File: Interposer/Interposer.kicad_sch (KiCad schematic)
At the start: 11 parts, among them J1 Cis_Electrode_In, J10 Trans_Electrode_Out, J11 Trans_Electrode_In, J2 Cis_Electrode_Out, P1 Port_Cis_In_30deg, P2 Port_Cis_Out_330deg, P3 Port_Trans_In_210deg, P4 Port_Trans_Out_150deg

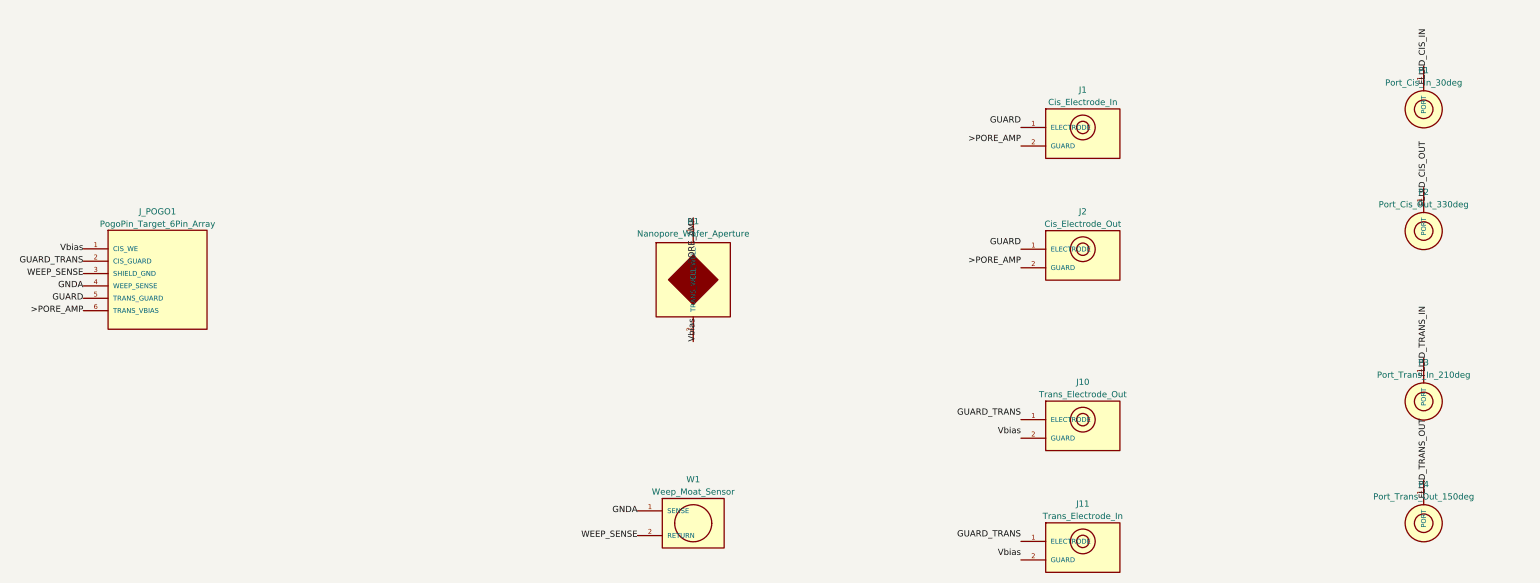
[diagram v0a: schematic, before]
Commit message: feat(interposer): implement 4-electrode concentric cell with Gamry terminology, EIS simulation, and KiCad models
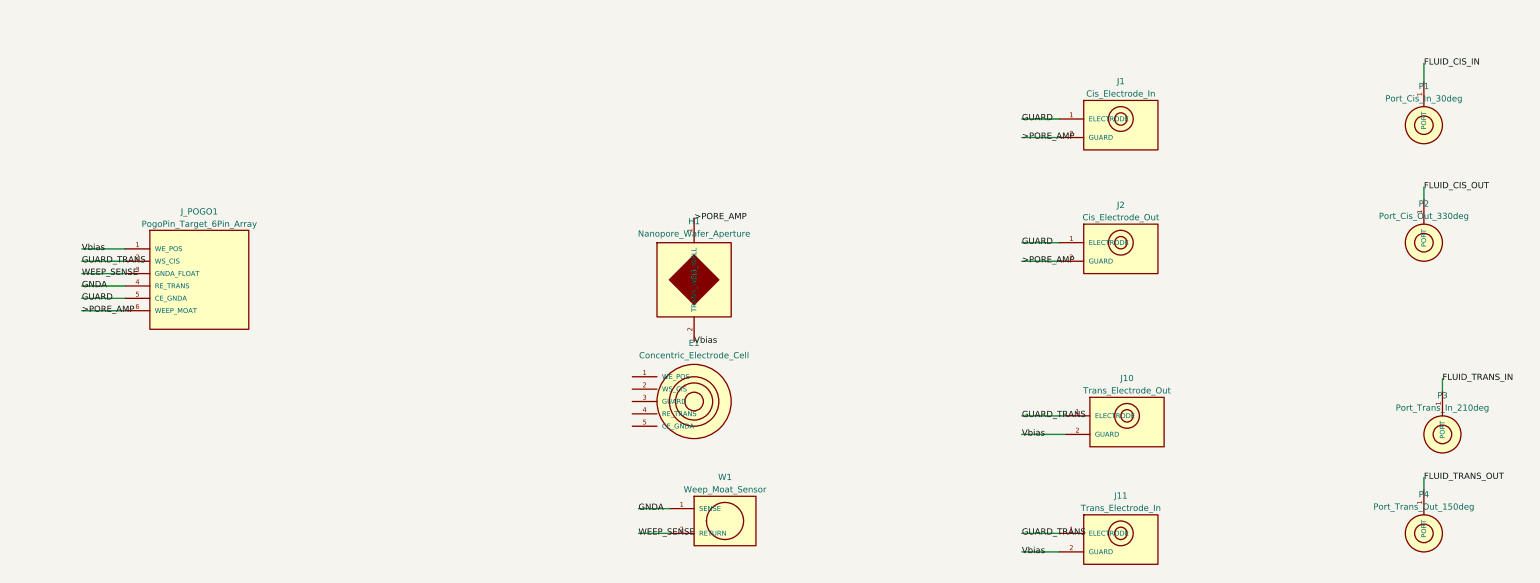
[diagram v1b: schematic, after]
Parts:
- added E1: Concentric_Electrode_Cell, footprints:Nanopore holder_recessed, symbol Interposer:Concentric_Electrode_Cell
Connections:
- net >PORE_AMP: now also J1.2 (GUARD), J2.2 (GUARD)
- net FLUID_CIS_IN: now also P1.1 (PORT)
- net FLUID_CIS_OUT: now also P2.1 (PORT)
- net FLUID_TRANS_IN: now also P3.1 (PORT)
- net FLUID_TRANS_OUT: now also P4.1 (PORT)
- net GUARD: now also J1.1 (ELECTRODE), J2.1 (ELECTRODE)
- net GUARD_TRANS: now also J10.1 (ELECTRODE), J11.1 (ELECTRODE)
- net Vbias: now also J10.2 (GUARD), J11.2 (GUARD)
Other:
- moved on the sheet: J1, J10, J11, J2, J_POGO1, P1, P2, P3, P4, W1

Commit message: refactor(interposer): reconcile 4-electrode cell with channel-aligned Ag/AgCl ribbons and Gamry pinout
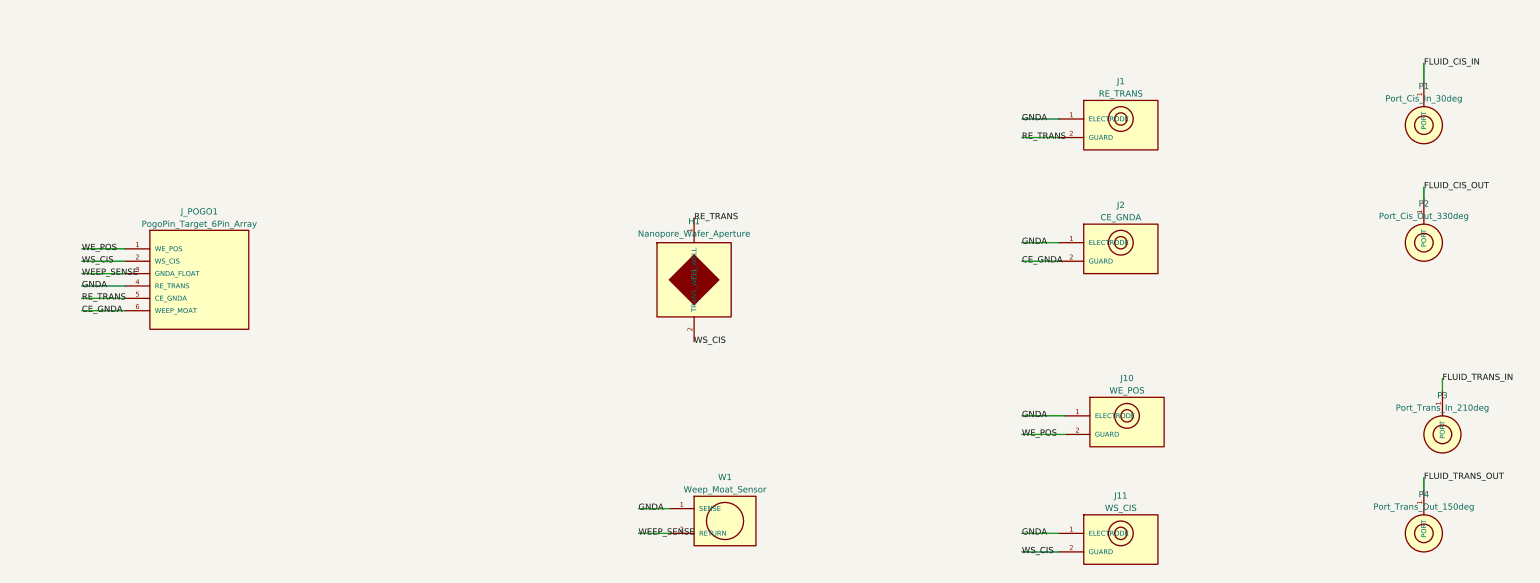
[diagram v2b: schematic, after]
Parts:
- removed E1: Concentric_Electrode_Cell, footprints:Nanopore holder_recessed, symbol Interposer:Concentric_Electrode_Cell
- J1: value Cis_Electrode_In -> RE_TRANS
- J10: value Trans_Electrode_Out -> WE_POS
- J11: value Trans_Electrode_In -> WS_CIS
- J2: value Cis_Electrode_Out -> CE_GNDA
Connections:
- net GNDA: now also J1.1 (ELECTRODE), J10.1 (ELECTRODE), J11.1 (ELECTRODE), J2.1 (ELECTRODE)
- net >PORE_AMP renamed CE_GNDA
- net CE_GNDA: no longer H1.1 (CIS_WELL), J1.2 (GUARD)
- removed net GUARD: J1.1 (ELECTRODE), J2.1 (ELECTRODE), J_POGO1.5 (CE_GNDA)
- removed net GUARD_TRANS: J10.1 (ELECTRODE), J11.1 (ELECTRODE), J_POGO1.2 (WS_CIS)
- net Vbias renamed WE_POS
- net WE_POS: no longer H1.2 (TRANS_WELL), J11.2 (GUARD)
- new net RE_TRANS: H1.1 (CIS_WELL), J1.2 (GUARD), J_POGO1.5 (CE_GNDA)
- new net WS_CIS: H1.2 (TRANS_WELL), J11.2 (GUARD), J_POGO1.2 (WS_CIS)
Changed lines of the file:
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@@
 		)
 	)
-	(label ">PORE_AMP"
+	(label "RE_TRANS"
 		(at 170.18 67.31 0)
 		(effects
@@
 		)
 	)
-	(label "GUARD_TRANS"
+	(label "GNDA"
 		(at 237.49 107.95 0)
 		(effects
@@
 		)
 	)
-	(label "Vbias"
+	(label "WS_CIS"
 		(at 237.49 135.89 0)
 		(effects
@@
 		)
 	)
-	(label ">PORE_AMP"
+	(label "CE_GNDA"
 		(at 237.49 76.2 0)
 		(effects
@@
 		)
 	)
-	(label "GUARD"
+	(label "RE_TRANS"
 		(at 44.45 83.82 0)
 		(effects
@@
 		)
 	)
-	(label "Vbias"
+	(label "WE_POS"
 		(at 44.45 73.66 0)
 		(effects
@@
 		)
 	)
-	(label "Vbias"
+	(label "WS_CIS"
 		(at 170.18 92.71 0)
 		(effects
@@
 		)
 	)
-	(label ">PORE_AMP"
+	(label "RE_TRANS"
 		(at 237.49 50.8 0)
 		(effects
@@
 		)
 	)
-	(label "GUARD"
+	(label "GNDA"
 		(at 237.49 46.99 0)
 		(effects
@@
 		)
 	)
-	(label "Vbias"
+	(label "WE_POS"
 		(at 237.49 111.76 0)
 		(effects
@@
 		)
 	)
-	(label "GUARD_TRANS"
+	(label "GNDA"
 		(at 237.49 132.08 0)
 		(effects
@@
 		)
 	)
-	(label ">PORE_AMP"
+	(label "CE_GNDA"
 		(at 44.45 86.36 0)
 		(effects
@@
 		)
 	)
-	(label "GUARD_TRANS"
+	(label "WS_CIS"
 		(at 44.45 76.2 0)
 		(effects
@@
 		)
 	)
-	(label "GUARD"
+	(label "GNDA"
 		(at 237.49 72.39 0)
 		(effects
@@
 			)
 		)
-		(property "Value" "Cis_Electrode_Out"
+		(property "Value" "CE_GNDA"
 			(at 257.81 67.2 0)
 			(show_name no)
@@
 			)
 		)
-		(property "Description" "Ag/AgCl Ribbon Electrode Pad (Cis Out, r=17mm) with Driven Guard Ring"
+		(property "Description" "Counter Electrode Pad (Ag/AgCl Ribbon, Trans Outer)"
 			(at 257.81 73.66 0)
 			(hide yes)
@@
 			)
 		)
-		(property "Value" "Cis_Electrode_In"
+		(property "Value" "RE_TRANS"
 			(at 257.81 41.8 0)
 			(show_name no)
@@
 			)
 		)
-		(property "Description" "Ag/AgCl Ribbon Electrode Pad (Cis In, r=12mm) with Driven Guard Ring"
+		(property "Description" "Reference Sense Electrode Pad (Ag/AgCl Ribbon, Trans Inner)"
 			(at 257.81 48.26 0)
 			(hide yes)
@@
 			)
 		)
-		(property "Value" "Trans_Electrode_In"
+		(property "Value" "WS_CIS"
 			(at 257.81 126.89 0)
 			(show_name no)
@@
 			)
 		)
-		(property "Description" "Ag/AgCl Ribbon Electrode Pad (Trans In, r=12mm) with Driven Guard Ring"
+		(property "Description" "Working Sense Electrode Pad (Ag/AgCl Ribbon, Cis Inner)"
 			(at 257.81 133.35 0)
 			(hide yes)
@@
 			)
 		)
-		(property "Value" "Trans_Electrode_Out"
+		(property "Value" "WE_POS"
 			(at 259.08 102.76 0)
 			(show_name no)
@@
 			)
 		)
-		(property "Description" "Ag/AgCl Ribbon Electrode Pad (Trans Out, r=17mm) with Driven Guard Ring"
+		(property "Description" "Working Electrode Pad (Ag/AgCl Ribbon, Cis Outer)"
 			(at 259.08 109.22 0)
 			(hide yes)
@@
 					(unit 1)
 				)
-			)
-		)
-	)
-	(symbol
-		(lib_id "Interposer:Concentric_Electrode_Cell")
-		(at 170.18 105.0 0)
-		(unit 1)
-		(body_style 1)
-		(exclude_from_sim no)
-		(in_bom yes)
-		(on_board yes)
-		(in_pos_files yes)
-		(dnp no)
-		(fields_autoplaced yes)
-		(property "Reference" "E1"
-			(at 170.18 93.0 0)
-			(show_name no)
-			(do_not_autoplace no)
-			(effects
-				(font
-					(size 1.27 1.27)
-				)
-			)
-		)
-		(property "Value" "Concentric_Electrode_Cell"
-			(at 170.18 95.54 0)
-			(show_name no)
-			(do_not_autoplace no)
-			(effects
-				(font
-					(size 1.27 1.27)
-				)
-			)
-		)
-		(property "Footprint" "footprints:Nanopore holder_recessed"
-			(at 170.18 105.0 0)
-			(hide yes)
-			(show_name no)
-			(do_not_autoplace no)
-			(effects
-				(font
-					(size 1.27 1.27)
-				)
-			)
-		)
-		(property "Datasheet" "https://pubs.acs.org/doi/10.1021/acs.jpcc.6b12543"
-			(at 170.18 105.0 0)
-			(hide yes)
-			(show_name no)
-			(do_not_autoplace no)
-			(effects
-				(font
-					(size 1.27 1.27)
-				)
-			)
-		)
-		(property "Description" "Four-Electrode Concentric Kelvin Electrochemical Cell (WE, WS, RE, CE, Guard)"
-			(at 170.18 105.0 0)
-			(hide yes)
-			(show_name no)
-			(do_not_autoplace no)
-			(effects
-				(font
-					(size 1.27 1.27)
-				)
-			)
-		)
-		(pin "1"
-		)
-		(pin "2"
-		)
-		(pin "3"
-		)
-		(pin "4"
-		)
-		(pin "5"
-		)
-		(instances
-			(project "Interposer"
-				(path "/0fac162c-ca5e-4358-934a-30718aa12176"
-					(reference "E1")
-					(unit 1)
-				)

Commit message: Update Interposer and Amplifier interfaces to 12-pin Guarded Pogo layout
Modifies `J_POGO1` (the mechanical interface bridging the active amplifier and
passive flowcell interposer) from a 6-pin linear array to a 12-pin layout.

This 12-pin architecture surrounds the ultra-high impedance signals (`WS_CIS`
and `RE_TRANS`) with explicitly driven `GUARD` pins. By flanking these sensitive
nodes with driven low-impedance guards across the mechanical pogo connection,
stray surface leakage across the FR4 and mating interfaces is intercepted and
bootstrapped.

Changes:
- Replaced 6-pin target array footprints with `PogoPin_Target_12Pin_Distributed`.
- Replaced 6-pin spring header footprints with `PogoPin_SpringHeader_12Pin_Distributed`.
- Updated KiCad footprint `.kicad_mod` files to feature 12 pads.
- Updated `scripts/build_interposer_kicad.py` to instantiate the new 12-pin generic connector symbols and bind to the correct footprints.
- Updated unit test assertions in `tests/test_interposer_kicad.py` to expect the new pin counts, names, and symbol mappings.

Co-authored-by: google-labs-jules[bot] <161369871+google-labs-jules[bot]@users.noreply.github.com>
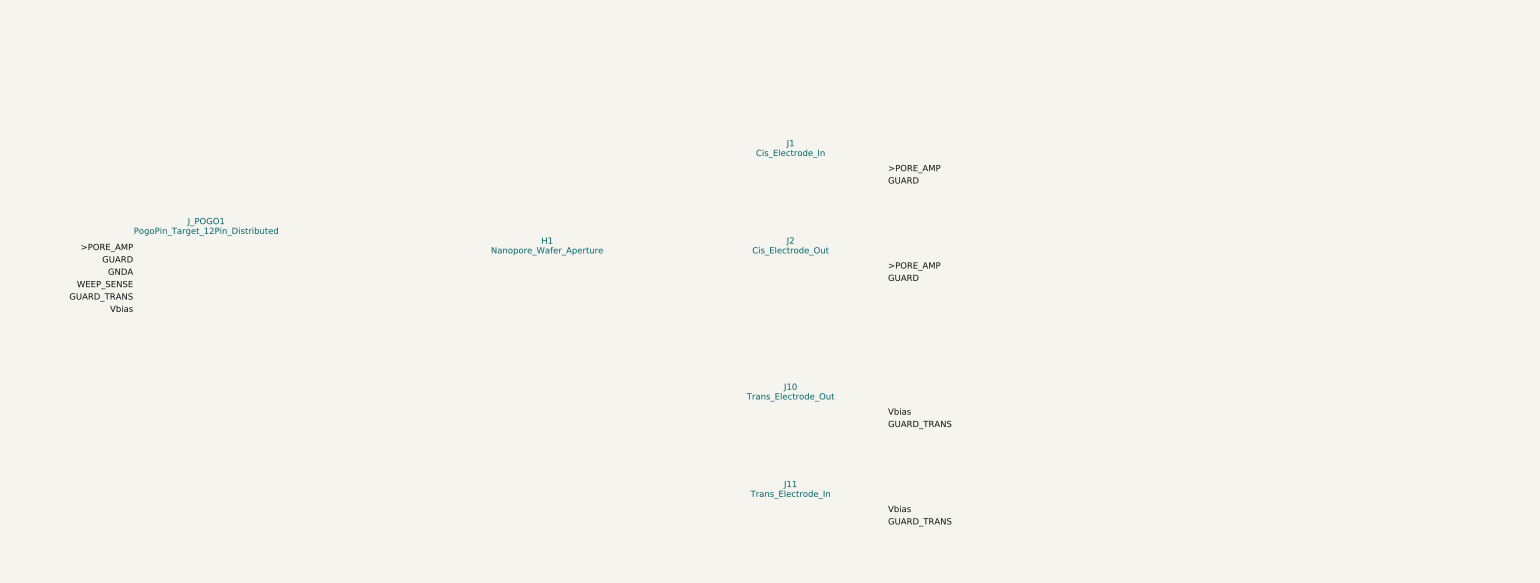
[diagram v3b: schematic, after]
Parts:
- removed H1: Nanopore_Wafer_Aperture, footprints:Nanopore holder_recessed, symbol Interposer:Nanopore_Wafer_Aperture
- removed J1: RE_TRANS, footprints:Electrode_Guard_Shield, symbol Interposer:Electrode_Guard_Shield
- removed J10: WE_POS, footprints:Electrode_Guard_Shield, symbol Interposer:Electrode_Guard_Shield
- removed J11: WS_CIS, footprints:Electrode_Guard_Shield, symbol Interposer:Electrode_Guard_Shield
- removed J2: CE_GNDA, footprints:Electrode_Guard_Shield, symbol Interposer:Electrode_Guard_Shield
- removed J_POGO1: PogoPin_Target_6Pin_Array, footprints:PogoPin_Target_6Pin_Array, symbol Interposer:PogoPin_Target_6Pin_Array
- removed P1: Port_Cis_In_30deg, symbol Interposer:Fluidic_Port_PassThrough
- removed P2: Port_Cis_Out_330deg, symbol Interposer:Fluidic_Port_PassThrough
- removed P3: Port_Trans_In_210deg, symbol Interposer:Fluidic_Port_PassThrough
- removed P4: Port_Trans_Out_150deg, symbol Interposer:Fluidic_Port_PassThrough
- removed W1: Weep_Moat_Sensor, symbol Interposer:Weep_Moat_Sensor
- added H1: Nanopore_Wafer_Aperture, footprints:Nanopore holder_recessed, symbol Mechanical:MountingHole
- added J1: Cis_Electrode_In, footprints:Electrode_Guard_Shield, symbol Connector_Generic:Conn_01x02
- added J10: Trans_Electrode_Out, footprints:Electrode_Guard_Shield, symbol Connector_Generic:Conn_01x02
- added J11: Trans_Electrode_In, footprints:Electrode_Guard_Shield, symbol Connector_Generic:Conn_01x02
- added J2: Cis_Electrode_Out, footprints:Electrode_Guard_Shield, symbol Connector_Generic:Conn_01x02
- added J_POGO1: PogoPin_Target_12Pin_Distributed, footprints:PogoPin_Target_12Pin_Distributed, symbol Connector_Generic:Conn_01x12

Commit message: refactor: Rename Daemon Pore/Sentinel to MR1 across codebase
- Replaced "Daemon Pore", "Sentinel", and related variations with "MR1" in files.
- Renamed files matching "sentinel" or "daemon-pore" to "mr1".
- Ensured file references, includes, makefiles, and render scripts are correctly pointed to the new names.
- Retained case formatting consistency (`MR1` for PascalCase/UPPER_CASE/Prose, `mr1` for snake_case/filenames).

Co-authored-by: google-labs-jules[bot] <161369871+google-labs-jules[bot]@users.noreply.github.com>
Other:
- company: Daemon Pore Open Source Nanopore Project -> MR1 Open Source Nanopore Project
- title: Daemon Pore - PTFE Microfluidic Interposer Board -> MR1 - PTFE Microfluidic Interposer Board
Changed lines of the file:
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@@
 	(paper "A4")
 	(title_block
-		(title "Daemon Pore - PTFE Microfluidic Interposer Board")
+		(title "MR1 - PTFE Microfluidic Interposer Board")
 		(date "2026-09-30")
 		(rev "1.0")
-		(company "Daemon Pore Open Source Nanopore Project")
+		(company "MR1 Open Source Nanopore Project")
 		(comment 1 "Passive Microfluidic Flow Cell Interposer & Electrode Pogo Interface")
 		(comment 2 "0.8mm Rogers RO4350B / PTFE Substrate (er=2.1, tan_delta=0.0002, ENIG Finish)")

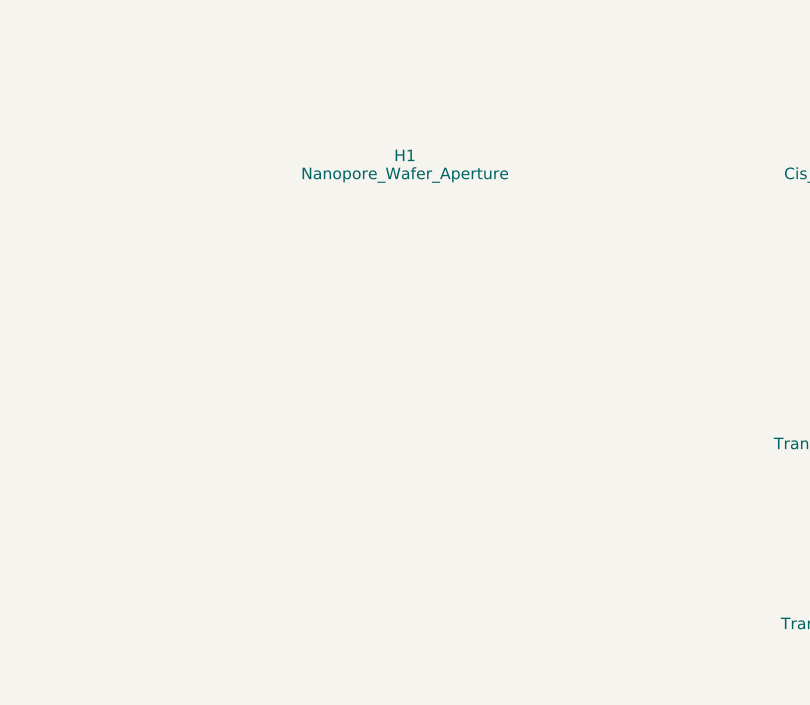
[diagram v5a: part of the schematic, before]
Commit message: fix(interposer): add missing H2-H4 holes and 12-pin pogo target array
Co-authored-by: google-labs-jules[bot] <161369871+google-labs-jules[bot]@users.noreply.github.com>
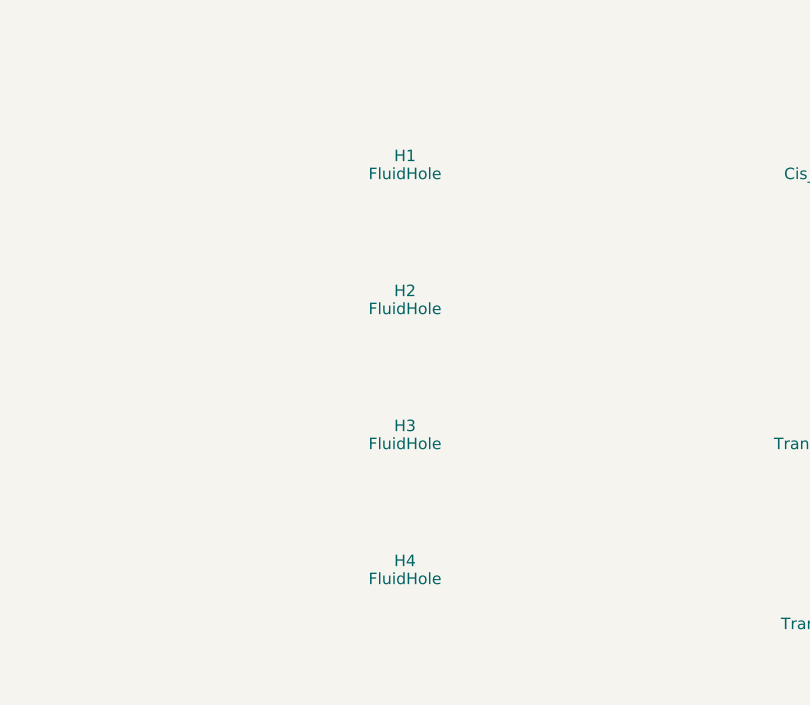
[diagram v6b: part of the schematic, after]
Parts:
- added H2, H3, H4: FluidHole, MountingHole:MountingHole_2.1mm, symbol Mechanical:MountingHole
- H1: value Nanopore_Wafer_Aperture -> FluidHole; footprint footprints:Nanopore holder_recessed -> MountingHole:MountingHole_2.1mm
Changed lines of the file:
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@@
 		(pin "5")
 		(pin "6")
+		(pin "7")
+		(pin "8")
+		(pin "9")
+		(pin "10")
+		(pin "11")
+		(pin "12")
 	)
 	(symbol (lib_id "Mechanical:MountingHole") (at 140.0 80.0 0) (unit 1)
 		(property "Reference" "H1" (at 140.0 72.0 0) (effects (font (size 1.27 1.27))))
-		(property "Value" "Nanopore_Wafer_Aperture" (at 140.0 74.0 0) (effects (font (size 1.27 1.27))))
-		(property "Footprint" "footprints:Nanopore holder_recessed" (at 140.0 80.0 0) (hide yes) (effects (font (size 1.27 1.27))))
+		(property "Value" "FluidHole" (at 140.0 74.0 0) (effects (font (size 1.27 1.27))))
+		(property "Footprint" "MountingHole:MountingHole_2.1mm" (at 140.0 80.0 0) (hide yes) (effects (font (size 1.27 1.27))))
+	)
+	(symbol (lib_id "Mechanical:MountingHole") (at 140.0 95.0 0) (unit 1)
+		(property "Reference" "H2" (at 140.0 87.0 0) (effects (font (size 1.27 1.27))))
+		(property "Value" "FluidHole" (at 140.0 89.0 0) (effects (font (size 1.27 1.27))))
+		(property "Footprint" "MountingHole:MountingHole_2.1mm" (at 140.0 95.0 0) (hide yes) (effects (font (size 1.27 1.27))))
+	)
+	(symbol (lib_id "Mechanical:MountingHole") (at 140.0 110.0 0) (unit 1)
+		(property "Reference" "H3" (at 140.0 102.0 0) (effects (font (size 1.27 1.27))))
+		(property "Value" "FluidHole" (at 140.0 104.0 0) (effects (font (size 1.27 1.27))))
+		(property "Footprint" "MountingHole:MountingHole_2.1mm" (at 140.0 110.0 0) (hide yes) (effects (font (size 1.27 1.27))))
+	)
+	(symbol (lib_id "Mechanical:MountingHole") (at 140.0 125.0 0) (unit 1)
+		(property "Reference" "H4" (at 140.0 117.0 0) (effects (font (size 1.27 1.27))))
+		(property "Value" "FluidHole" (at 140.0 119.0 0) (effects (font (size 1.27 1.27))))
+		(property "Footprint" "MountingHole:MountingHole_2.1mm" (at 140.0 125.0 0) (hide yes) (effects (font (size 1.27 1.27))))
 	)
 	(symbol (lib_id "Connector_Generic:Conn_01x02") (at 190.0 60.0 0) (unit 1)
